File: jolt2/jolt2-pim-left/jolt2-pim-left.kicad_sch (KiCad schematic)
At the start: 0 parts

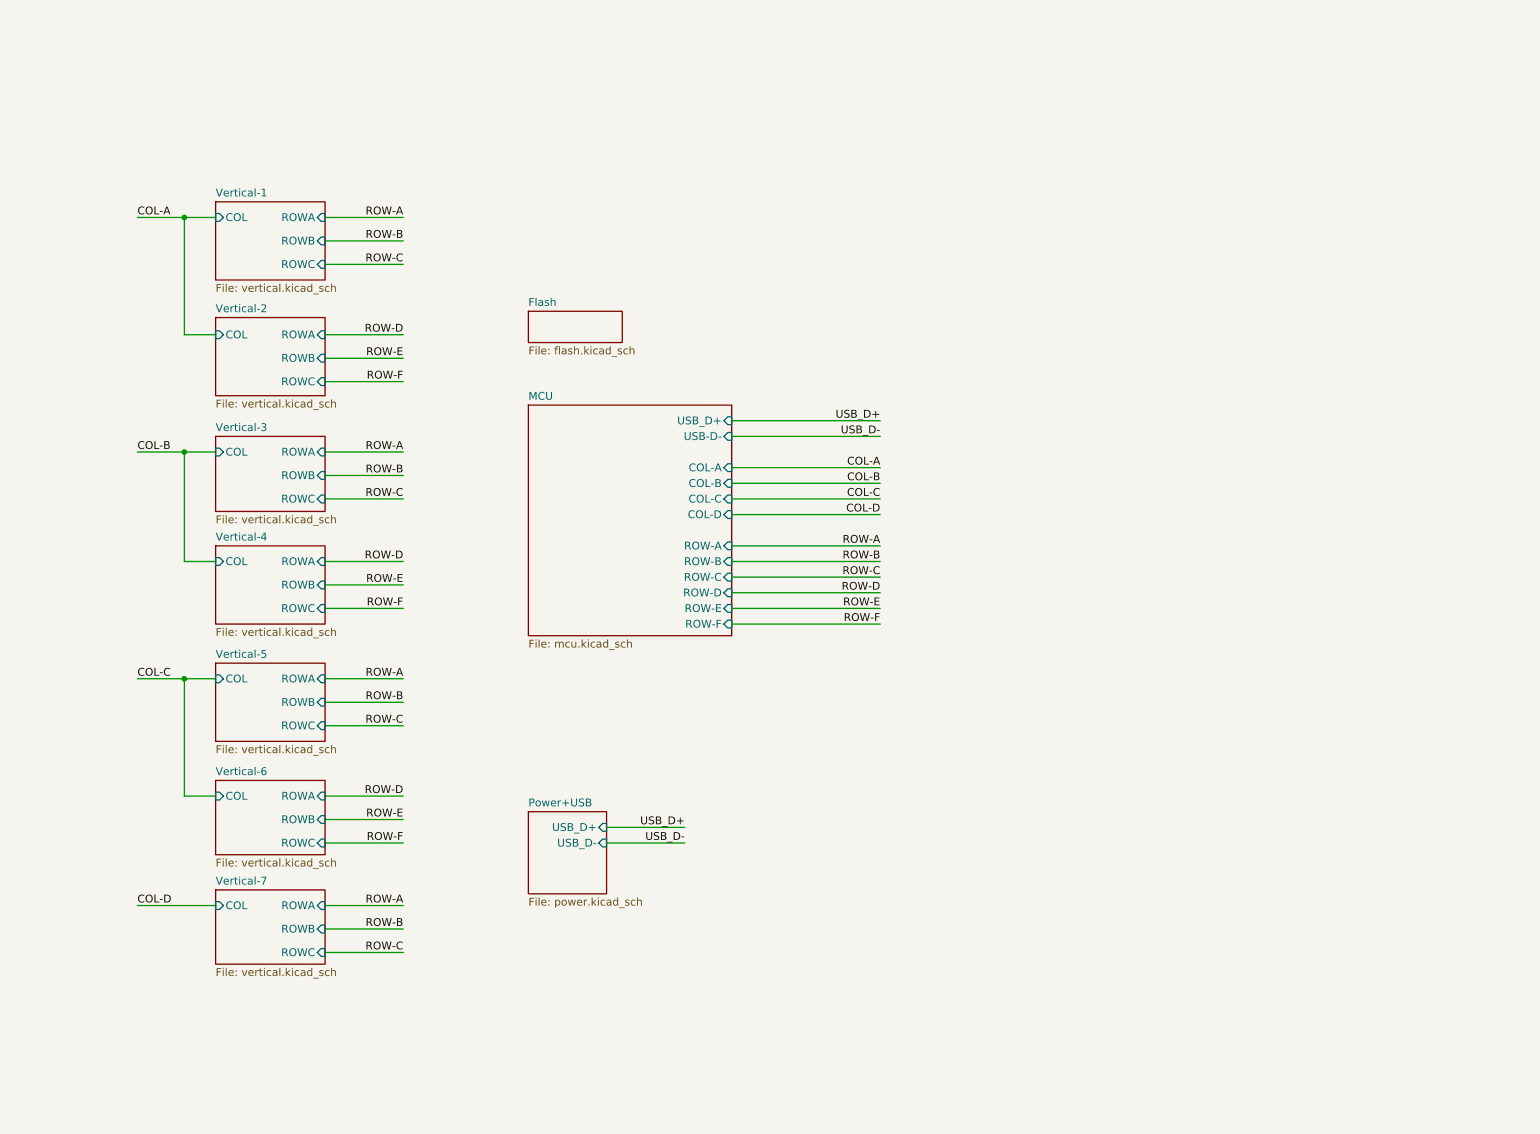
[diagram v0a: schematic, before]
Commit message: jolt2-pim-left: Finalize routing
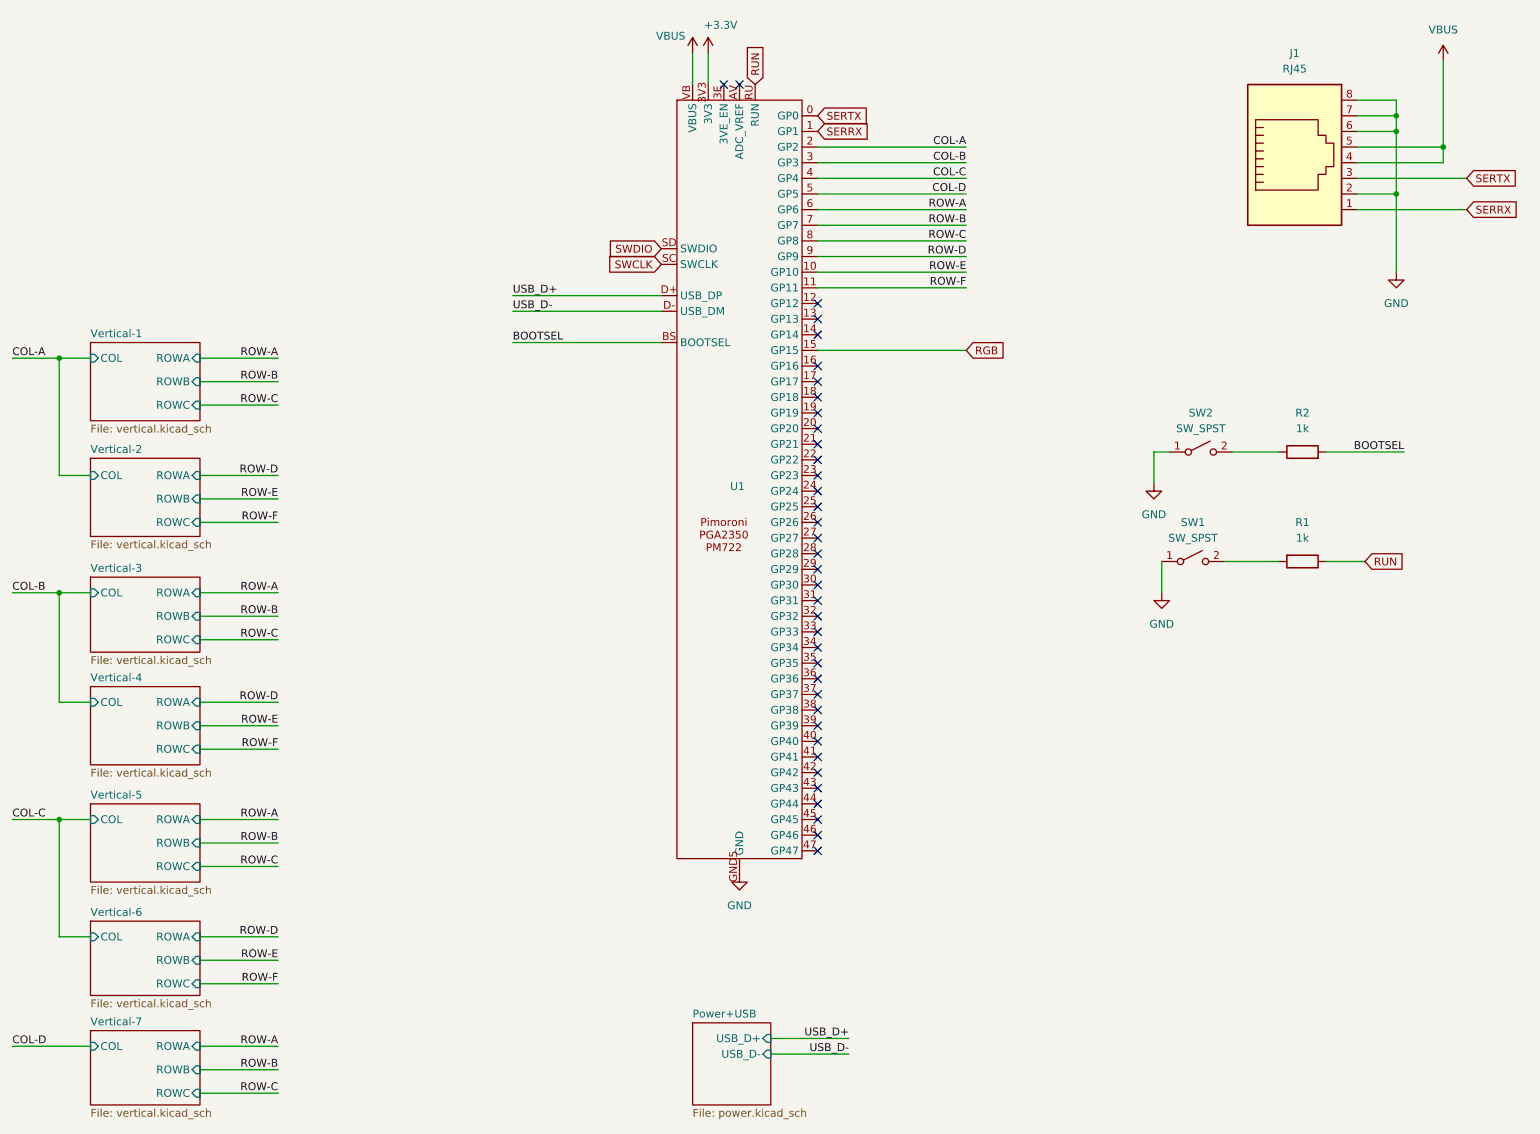
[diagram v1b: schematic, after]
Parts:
- added J1: RJ45, Connector_RJ:RJ45_Amphenol_54602-x08_Horizontal, symbol Connector:RJ45
- added R1, R2: 1k, Resistor_SMD:R_0603_1608Metric, symbol Device:R
- added SW1, SW2: SW_SPST, Button_Switch_SMD:SW_Push_1P1T_NO_CK_KMR2, symbol Switch:SW_SPST
- added U1: ~, davidb-keyboard-foot:PIMORONI-PGA2035-PM722, symbol David Brown Keyboard Parts:Pimoroni-PGA2350-PM722
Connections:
- net COL-A: now also U1.2 (GP2)
- net COL-B: now also U1.3 (GP3)
- net COL-C: now also U1.4 (GP4)
- net COL-D: now also U1.5 (GP5)
- net ROW-A: now also U1.6 (GP6)
- net ROW-B: now also U1.7 (GP7)
- net ROW-C: now also U1.8 (GP8)
- net ROW-D: now also U1.9 (GP9)
- net ROW-E: now also U1.10 (GP10)
- net ROW-F: now also U1.11 (GP11)
- net USB_D+: now also U1.D+ (USB_DP)
- net USB_D-: now also U1.D- (USB_DM)
- new net: R1.2, SW1.2 (B)
- new net: R2.1, SW2.2 (B)
- new net +3.3V: U1.3V3
- new net BOOTSEL: R2.2, U1.BS (BOOTSEL)
- new net GND: J1.2, J1.6, J1.7, J1.8, SW1.1 (A), SW2.1 (A), U1.GND1 (GND), U1.GND2 (GND), U1.GND3 (GND), U1.GND4 (GND), U1.GND5 (GND), U1.GND6 (GND)
- new net RGB: U1.15 (GP15)
- new net RUN: R1.1, U1.RU (RUN)
- new net SERRX: J1.1, U1.1 (GP1)
- new net SERTX: J1.3, U1.0 (GP0)
- new net SWCLK: U1.SC (SWCLK)
- new net SWDIO: U1.SD (SWDIO)
- new net VBUS: J1.4, J1.5, U1.VB (VBUS)
- no-connect marks 0 -> 37
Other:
- removed sheet Flash
- removed sheet MCU

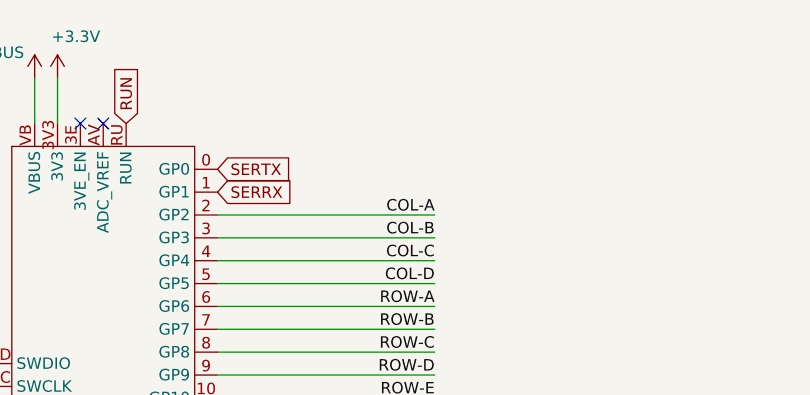
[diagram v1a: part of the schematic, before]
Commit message: jolt2-pim-left: Add uart terminating resistors
Place 27 ohm series resisters on the inter-board uart lines.
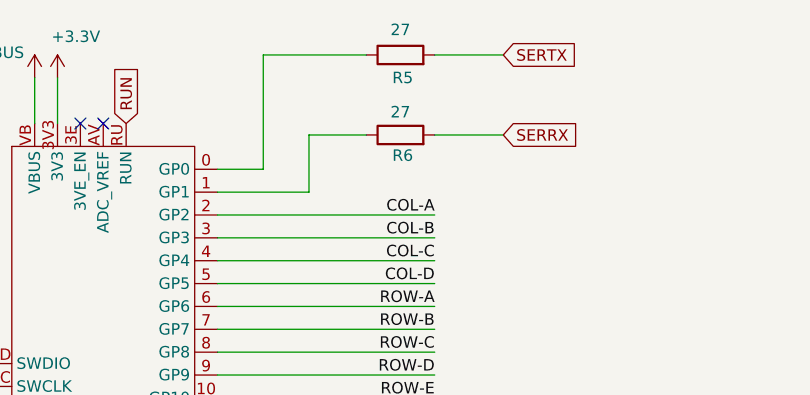
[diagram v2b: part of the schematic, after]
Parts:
- added R5, R6: 27, Resistor_SMD:R_0603_1608Metric_Pad0.98x0.95mm_HandSolder, symbol Device:R
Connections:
- net SERRX: now also R6.2; no longer U1.1 (GP1)
- net SERTX: now also R5.2; no longer U1.0 (GP0)
- new net: R5.1, U1.0 (GP0)
- new net: R6.1, U1.1 (GP1)
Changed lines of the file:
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@@
+	(wire
+		(pts
+			(xy 172.72 21.59) (xy 180.34 21.59)
+		)
+		(stroke
+			(width 0)
+			(type default)
+		)
+	)
+	(wire
+		(pts
+			(xy 158.75 30.48) (xy 165.1 30.48)
+		)
+		(stroke
+			(width 0)
+			(type default)
+		)
+	)
 	(wire
 		(pts
@@
 	(wire
 		(pts
+			(xy 165.1 21.59) (xy 153.67 21.59)
+		)
+		(stroke
+			(width 0)
+			(type default)
+		)
+	)
+	(wire
+		(pts
 			(xy 17.78 111.76) (xy 25.4 111.76)
 		)
@@
 	(wire
 		(pts
+			(xy 153.67 34.29) (xy 148.59 34.29)
+		)
+		(stroke
+			(width 0)
+			(type default)
+		)
+	)
+	(wire
+		(pts
 			(xy 17.78 73.66) (xy 25.4 73.66)
 		)
@@
 	(wire
 		(pts
+			(xy 153.67 21.59) (xy 153.67 34.29)
+		)
+		(stroke
+			(width 0)
+			(type default)
+		)
+	)
+	(wire
+		(pts
 			(xy 17.78 148.59) (xy 25.4 148.59)
 		)
@@
 	(wire
 		(pts
+			(xy 158.75 36.83) (xy 158.75 30.48)
+		)
+		(stroke
+			(width 0)
+			(type default)
+		)
+	)
+	(wire
+		(pts
 			(xy 48.26 193.04) (xy 60.96 193.04)
+		)
+		(stroke
+			(width 0)
+			(type default)
+		)
+	)
+	(wire
+		(pts
+			(xy 148.59 36.83) (xy 158.75 36.83)
+		)
+		(stroke
+			(width 0)
+			(type default)
+		)
+	)
+	(wire
+		(pts
+			(xy 172.72 30.48) (xy 180.34 30.48)
 		)
 		(stroke
@@
 	(global_label "SERRX"
 		(shape input)
-		(at 148.59 36.83 0)
+		(at 180.34 30.48 0)
 		(fields_autoplaced yes)
 		(effects
@@
 		)
 		(property "Intersheetrefs" "${INTERSHEET_REFS}"
-			(at 157.6832 36.83 0)
+			(at 189.4332 30.48 0)
 			(effects
 				(font
@@
 	(global_label "SERTX"
 		(shape input)
-		(at 148.59 34.29 0)
+		(at 180.34 21.59 0)
 		(fields_autoplaced yes)
 		(effects
@@
 		)
 		(property "Intersheetrefs" "${INTERSHEET_REFS}"
-			(at 157.3808 34.29 0)
+			(at 189.1308 21.59 0)
 			(effects
 				(font
@@
 	)
 	(symbol
+		(lib_id "Device:R")
+		(at 168.91 21.59 90)
+		(unit 1)
+		(exclude_from_sim no)
+		(in_bom yes)
+		(on_board yes)
+		(dnp no)
+		(property "Reference" "R5"
+			(at 169.164 24.13 90)
+			(effects
+				(font
+					(size 1.27 1.27)
+				)
+			)
+		)
+		(property "Value" "27"
+			(at 168.91 18.796 90)
+			(effects
+				(font
+					(size 1.27 1.27)
+				)
+			)
+		)
+		(property "Footprint" "Resistor_SMD:R_0603_1608Metric_Pad0.98x0.95mm_HandSolder"
+			(at 168.91 23.368 90)
+			(effects
+				(font
+					(size 1.27 1.27)
+				)
+				(hide yes)
+			)
+		)
+		(property "Datasheet" "~"
+			(at 168.91 21.59 0)
+			(effects
+				(font
+					(size 1.27 1.27)
+				)
+				(hide yes)
+			)
+		)
+		(property "Description" "Resistor"
+			(at 168.91 21.59 0)
+			(effects
+				(font
+					(size 1.27 1.27)
+				)
+				(hide yes)
+			)
+		)
+		(pin "1"
+		)
+		(pin "2"
+		)
+		(instances
+			(project ""
+				(path "/5e404b8e-7f18-4204-bb67-87c83d2db771"
+					(reference "R5")
+					(unit 1)
+				)
+			)
+		)
+	)
+	(symbol
 		(lib_id "power:GND")
 		(at 135.89 157.48 0)
@@
 					(unit 1)
 				)
+			)
+		)
+	)
+	(symbol
+		(lib_id "Device:R")
+		(at 168.91 30.48 90)
+		(unit 1)
+		(exclude_from_sim no)
+		(in_bom yes)
+		(on_board yes)
+		(dnp no)
+		(property "Reference" "R6"
+			(at 169.164 32.766 90)
+			(effects
+				(font
+					(size 1.27 1.27)
+				)
+			)
+		)
+		(property "Value" "27"
+			(at 168.91 27.94 90)
+			(effects
+				(font
+					(size 1.27 1.27)
+				)
+			)
+		)
+		(property "Footprint" "Resistor_SMD:R_0603_1608Metric_Pad0.98x0.95mm_HandSolder"
+			(at 168.91 32.258 90)
+			(effects
+				(font
+					(size 1.27 1.27)
+				)
+				(hide yes)
+			)
+		)
+		(property "Datasheet" "~"
+			(at 168.91 30.48 0)
+			(effects
+				(font
+					(size 1.27 1.27)
+				)
+				(hide yes)
+			)
+		)
+		(property "Description" "Resistor"
+			(at 168.91 30.48 0)
+			(effects
+				(font
+					(size 1.27 1.27)
+				)
+				(hide yes)
+			)
+		)
+		(pin "1"
+		)
+		(pin "2"
+		)
+		(instances
+			(project ""
+				(path "/5e404b8e-7f18-4204-bb67-87c83d2db771"
+					(reference "R6")
+					(unit 1)
+				)
